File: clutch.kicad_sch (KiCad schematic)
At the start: 1 part, among them J10 Clutch

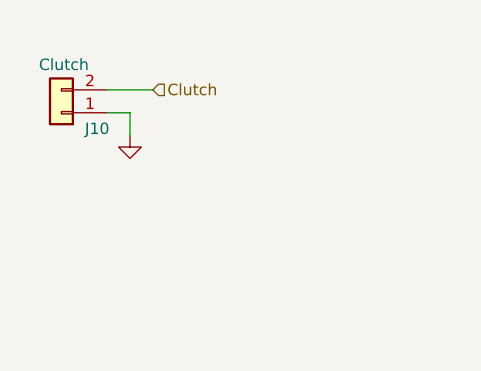
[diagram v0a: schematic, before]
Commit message: Add MOSFET to switch a relay on the clutch output
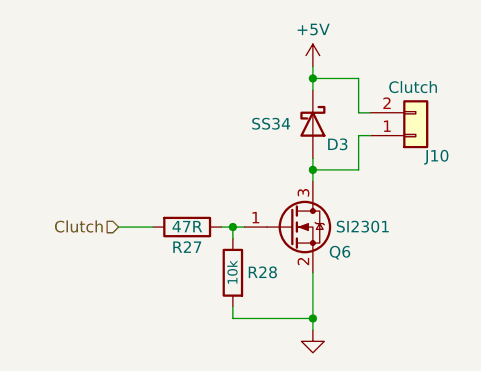
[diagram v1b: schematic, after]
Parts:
- added D3: SS34, Diode_SMD:D_SMA, symbol Diode:SS34
- added Q6: SI2301, Package_TO_SOT_SMD:SOT-23, symbol Device:Q_NMOS_GSD
- added R27: 47R, Resistor_SMD:R_0805_2012Metric, symbol Device:R
- added R28: 10k, Resistor_SMD:R_0805_2012Metric, symbol Device:R
- J10: LCSC (none) -> C7434479
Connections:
- net Clutch: now also R27.2; no longer J10.2 (Pin_2)
- net GND: now also Q6.2 (S), R28.2; no longer J10.1 (Pin_1)
- new net: Q6.1 (G), R27.1, R28.1
- new net: D3.2 (A), J10.1 (Pin_1), Q6.3 (D)
- new net +5V: D3.1 (K), J10.2 (Pin_2)
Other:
- moved on the sheet: J10

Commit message: Tweaks to hand-load components for current availability
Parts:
- J10: LCSC C7434479 -> C7494857
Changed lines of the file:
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@@
 			)
 		)
-		(property "LCSC" "C7434479"
+		(property "LCSC" "C7494857"
 			(at 157.48 101.6 0)
 			(effects
